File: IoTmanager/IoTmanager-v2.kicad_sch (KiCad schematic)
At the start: 63 parts, among them J2 Conn_01x12_Pin, J3 Conn_01x12_Pin, J4-flash1 flash, J5 reset, K3 ZC32F-012-HS3-copy, K5 ZC32F-012-HS3-copy, K6 ZC32F-012-HS3-copy, K7 ZC32F-012-HS3-copy, Q1-pnp1 MMBT5401, Q10-pnp1 MMBT5401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

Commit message: update
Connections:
- net +12C: now also J2.3 (Pin_3); no longer J2.12 (Pin_12)
- net +3.3V: now also J2.5 (Pin_5)
- net +5C: now also J2.4 (Pin_4); no longer J2.2 (Pin_2)
- net GNDPWR: now also J2.2 (Pin_2)
- net d8: now also J2.12 (Pin_12); no longer J2.5 (Pin_5)
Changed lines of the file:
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@@
 	)
 	(label "d8"
-		(at 264.16 160.02 0)
+		(at 269.24 177.8 0)
 		(fields_autoplaced yes)
 		(effects
@@
 	(symbol
 		(lib_id "power:+12C")
-		(at 269.24 177.8 270)
+		(at 264.16 154.94 270)
 		(unit 1)
 		(exclude_from_sim no)
@@
 		(fields_autoplaced yes)
 		(property "Reference" "#PWR033"
-			(at 265.43 177.8 0)
+			(at 260.35 154.94 0)
 			(effects
 				(font
@@
 		)
 		(property "Value" "+12C"
-			(at 273.05 177.7999 90)
+			(at 267.97 154.9399 90)
 			(effects
 				(font
@@
 		)
 		(property "Footprint" ""
-			(at 269.24 177.8 0)
+			(at 264.16 154.94 0)
 			(effects
 				(font
@@
 		)
 		(property "Datasheet" ""
-			(at 269.24 177.8 0)
+			(at 264.16 154.94 0)
 			(effects
 				(font
@@
 		)
 		(property "Description" "Power symbol creates a global label with name \"+12C\""
-			(at 269.24 177.8 0)
+			(at 264.16 154.94 0)
 			(effects
 				(font
@@
 	)
 	(symbol
+		(lib_id "power:+3.3V")
+		(at 264.16 160.02 270)
+		(unit 1)
+		(exclude_from_sim no)
+		(in_bom yes)
+		(on_board yes)
+		(dnp no)
+		(fields_autoplaced yes)
+		(property "Reference" "#PWR036"
+			(at 260.35 160.02 0)
+			(effects
+				(font
+					(size 1.27 1.27)
+				)
+				(hide yes)
+			)
+		)
+		(property "Value" "+3.3V"
+			(at 267.97 160.0199 90)
+			(effects
+				(font
+					(size 1.27 1.27)
+				)
+				(justify left)
+			)
+		)
+		(property "Footprint" ""
+			(at 264.16 160.02 0)
+			(effects
+				(font
+					(size 1.27 1.27)
+				)
+				(hide yes)
+			)
+		)
+		(property "Datasheet" ""
+			(at 264.16 160.02 0)
+			(effects
+				(font
+					(size 1.27 1.27)
+				)
+				(hide yes)
+			)
+		)
+		(property "Description" "Power symbol creates a global label with name \"+3.3V\""
+			(at 264.16 160.02 0)
+			(effects
+				(font
+					(size 1.27 1.27)
+				)
+				(hide yes)
+			)
+		)
+		(pin "1"
+		)
+		(instances
+			(project "IoTmanager-v2"
+				(path "/e30adb8f-2050-4707-a23b-b56498f87e6f"
+					(reference "#PWR036")
+					(unit 1)
+				)
+			)
+		)
+	)
+	(symbol
 		(lib_id "power:GNDPWR")
 		(at 60.96 71.12 0)
@@
 	)
 	(symbol
+		(lib_id "power:GNDPWR")
+		(at 264.16 152.4 90)
+		(unit 1)
+		(exclude_from_sim no)
+		(in_bom yes)
+		(on_board yes)
+		(dnp no)
+		(fields_autoplaced yes)
+		(property "Reference" "#PWR045"
+			(at 269.24 152.4 0)
+			(effects
+				(font
+					(size 1.27 1.27)
+				)
+				(hide yes)
+			)
+		)
+		(property "Value" "GNDPWR"
+			(at 267.97 152.5269 90)
+			(effects
+				(font
+					(size 1.27 1.27)
+				)
+				(justify right)
+			)
+		)
+		(property "Footprint" ""
+			(at 265.43 152.4 0)
+			(effects
+				(font
+					(size 1.27 1.27)
+				)
+				(hide yes)
+			)
+		)
+		(property "Datasheet" ""
+			(at 265.43 152.4 0)
+			(effects
+				(font
+					(size 1.27 1.27)
+				)
+				(hide yes)
+			)
+		)
+		(property "Description" "Power symbol creates a global label with name \"GNDPWR\" , global ground"
+			(at 264.16 152.4 0)
+			(effects
+				(font
+					(size 1.27 1.27)
+				)
+				(hide yes)
+			)
+		)
+		(pin "1"
+		)
+		(instances
+			(project "IoTmanager-v2"
+				(path "/e30adb8f-2050-4707-a23b-b56498f87e6f"
+					(reference "#PWR045")
+					(unit 1)
+				)
+			)
+		)
+	)
+	(symbol
 		(lib_id "power:+3.3V")
 		(at 182.88 279.4 0)
@@
 	(symbol
 		(lib_id "power:+5C")
-		(at 264.16 152.4 270)
+		(at 264.16 157.48 270)
 		(unit 1)
 		(exclude_from_sim no)
@@
 		(fields_autoplaced yes)
 		(property "Reference" "#PWR09"
-			(at 260.35 152.4 0)
+			(at 260.35 157.48 0)
 			(effects
 				(font
@@
 		)
 		(property "Value" "+5C"
-			(at 267.97 152.3999 90)
+			(at 267.97 157.4799 90)
 			(effects
 				(font
@@
 		)
 		(property "Footprint" ""
-			(at 264.16 152.4 0)
+			(at 264.16 157.48 0)
 			(effects
 				(font
@@
 		)
 		(property "Datasheet" ""
-			(at 264.16 152.4 0)
+			(at 264.16 157.48 0)
 			(effects
 				(font
@@
 		)
 		(property "Description" "Power symbol creates a global label with name \"+5C\""
-			(at 264.16 152.4 0)
+			(at 264.16 157.48 0)
 			(effects
 				(font

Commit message: update
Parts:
- added C2: C_Polarized_1000mF, Capacitor_THT:CP_Radial_D10.0mm_P3.50mm, symbol resistor:C_Polarized_Small
- added D6: LED, LED_THT:LED_D5.0mm, symbol Device:LED
- added R10: R-150, Resistor_SMD:R_0805_2012Metric, symbol models:R-100
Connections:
- net +5C: now also C2.1, D6.2 (A)
- net GNDPWR: now also C2.2, R10.2
- new net: D6.1 (K), R10.1

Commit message: update
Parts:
- added R12-10k2, R12-10k3: R-1k, Resistor_SMD:R_0805_2012Metric, symbol models:R-10k
- added U3: DHT11, Sensor:Aosong_DHT11_5.5x12.0_P2.54mm, symbol Sensor:DHT11
- U1, U4: now not fitted
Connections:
- net +5C: now also U3.1 (VDD)
- net GNDPWR: now also U3.4 (GND)
- net d0: no longer J2.9 (Pin_9)
- net d1: now also U3-tsop23.1 (OUT), R12-10k3.2; no longer U2.20 (GPIO5)
- net d2: now also R12-10k2.2; no longer U2.19 (GPIO4)
- net d4: now also U3.2 (DATA)
- net d5: no longer Jumper-d5.1, U3-tsop23.1 (OUT)
- net d6: no longer Jumper-d6.1
- net d7: no longer Jumper-d7.1
- net at IRLR1.1 (G), R5.2, R6.2: now also Jumper-d6.1
- net at IRLR3.1 (G), R8.2, R9.2: now also Jumper-d7.1
- net at IRLR2.1 (G), R1.2, R2.2: now also Jumper-d5.1
- new net: R12-10k3.1, U2.20 (GPIO5)
- new net: R12-10k2.1, U2.19 (GPIO4)
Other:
- moved on the sheet: IRLR3, Jumper-d5, Jumper-d6, Jumper-d7, R5, R8, R9

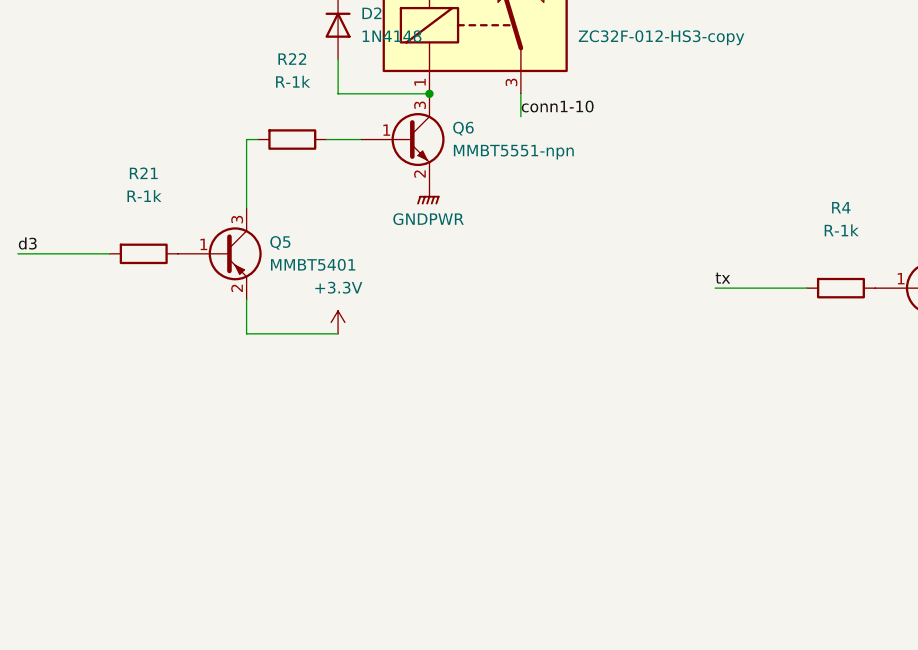
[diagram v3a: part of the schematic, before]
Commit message: Update IoTmanager schematic and libraries
- Changed paper size from A3 to A2 in IoTmanager schematic.
- Added MMDT4413-7-F symbol and footprint to the schematic and libraries.
- Updated various component properties including reference, value, and footprint.
- Adjusted component placements and added new power symbols for +3.3V and GNDPWR.
- Modified existing project files in Proteous tests, including autosaved versions.
- Updated fp-info-cache with new component details.
- Created new KiCAD symbol and footprint files for MMDT4413-7-F.
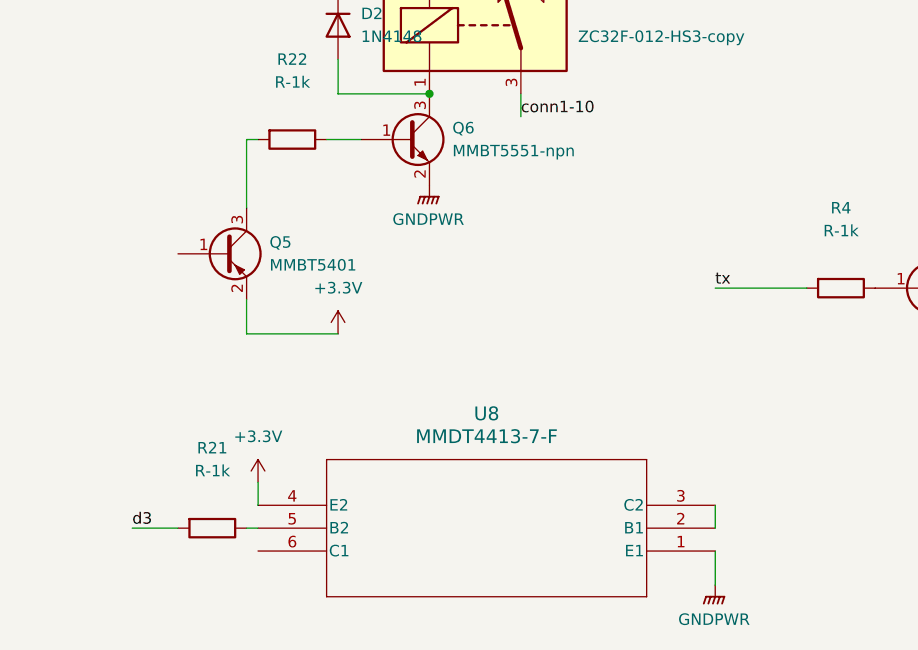
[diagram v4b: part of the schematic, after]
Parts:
- added U8: MMDT4413-7-F, module-custom-for-esp8266:SOT-363_DIO, symbol models:MMDT4413-7-F
- U3-tsop23: footprint OptoDevice:Vishay_MOLD-3Pin -> module-custom-for-esp8266:Vishay_MINIMOLD-3Pin_GND_correct
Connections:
- net +3.3V: now also U8.4 (E2)
- net GNDPWR: now also U8.1 (E1)
- net at R21.1: now also U8.5 (B2); no longer Q5.1 (B)
- new net: U8.2 (B1), U8.3 (C2)
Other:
- moved on the sheet: R21

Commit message: auto update from EPAM computer
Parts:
- added C3: C_Small, Capacitor_SMD:C_0805_2012Metric_Pad1.18x1.45mm_HandSolder, symbol Device:C_Small
- added R11: R-100, Resistor_SMD:R_0805_2012Metric, symbol models:R-100
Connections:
- net +5C: now also C3.1
- net GNDPWR: now also C3.2
- net d1: now also R11.2; no longer U3-tsop23.1 (OUT)
- net d2: now also R16.2
- net d8: no longer R16.2
- new net: R11.1, U3-tsop23.1 (OUT)

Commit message: update
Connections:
- net d3: now also Q5.1 (B)
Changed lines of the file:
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@@
 	(wire
 		(pts
-			(xy 161.29 180.34) (xy 163.83 180.34)
+			(xy 240.03 128.27) (xy 245.11 128.27)
 		)
 		(stroke
@@
 	(wire
 		(pts
-			(xy 240.03 128.27) (xy 245.11 128.27)
+			(xy 138.43 180.34) (xy 153.67 180.34)
 		)
 		(stroke
@@
 	(wire
 		(pts
-			(xy 138.43 180.34) (xy 153.67 180.34)
-		)
-		(stroke
-			(width 0)
-			(type default)
-		)
-	)
-	(wire
-		(pts
 			(xy 140.97 123.19) (xy 148.59 123.19)
 		)
@@
 	(wire
 		(pts
+			(xy 15.24 262.89) (xy 20.32 262.89)
+		)
+		(stroke
+			(width 0)
+			(type default)
+		)
+	)
+	(wire
+		(pts
 			(xy 135.89 248.92) (xy 135.89 251.46)
 		)
@@
 	(wire
 		(pts
+			(xy 163.83 180.34) (xy 161.29 180.34)
+		)
+		(stroke
+			(width 0)
+			(type default)
+		)
+	)
+	(wire
+		(pts
 			(xy 139.7 97.79) (xy 139.7 100.33)
 		)
@@
 		)
 	)
+	(label "d3"
+		(at 15.24 262.89 0)
+		(fields_autoplaced yes)
+		(effects
+			(font
+				(size 1.27 1.27)
+			)
+			(justify left bottom)
+		)
+	)
 	(label "conn2-9"
 		(at 265.43 210.82 0)
@@
 		(on_board yes)
 		(dnp no)
-		(fields_autoplaced yes)
 		(property "Reference" "R21"
-			(at 24.13 284.48 90)
+			(at 24.13 289.052 90)
 			(effects
 				(font
@@
 		)
 		(property "Value" "R-1k"
-			(at 24.13 287.02 90)
+			(at 24.384 290.83 90)
 			(effects
 				(font
@@
 					(size 1.27 1.27)
 				)
+				(hide yes)
 			)
 		)

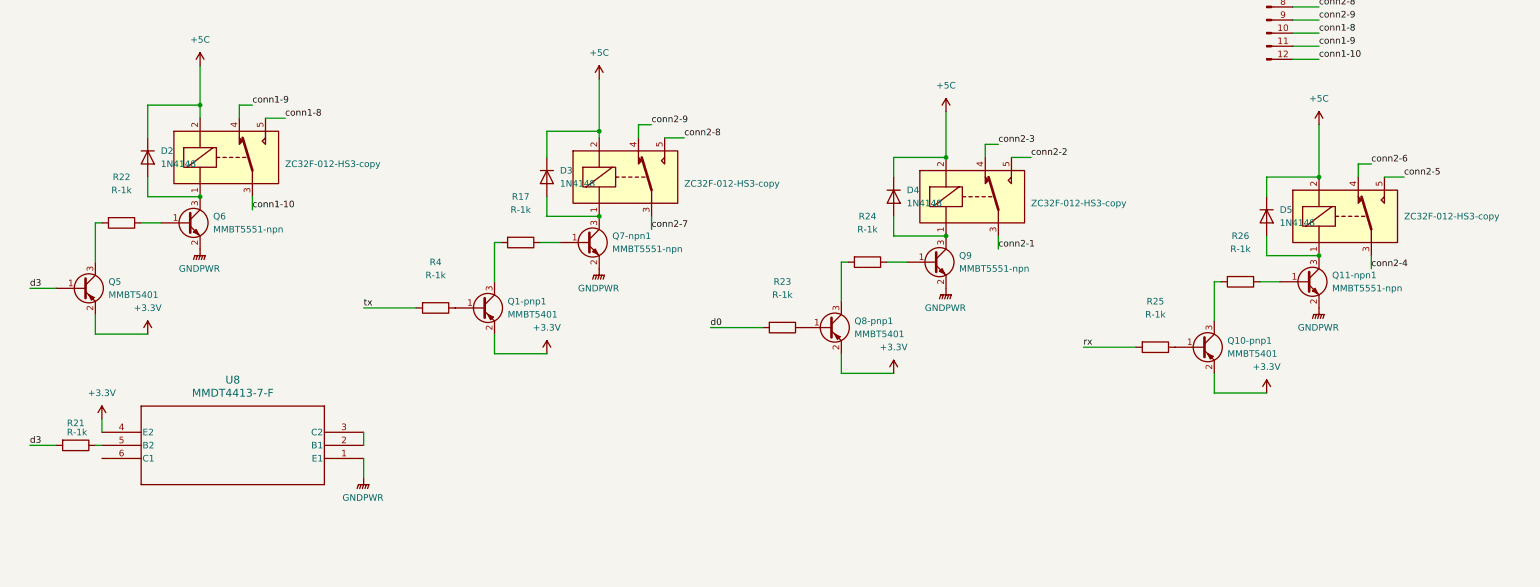
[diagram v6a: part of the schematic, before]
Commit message: Update fp-info-cache with new audio module and relay specifications
- Updated the ID for the Audio_Module entry.
- Added new relay module (RELAY_SRD-05VDC-SL-C) with specifications.
- Ensured proper formatting and consistency in the module entries.
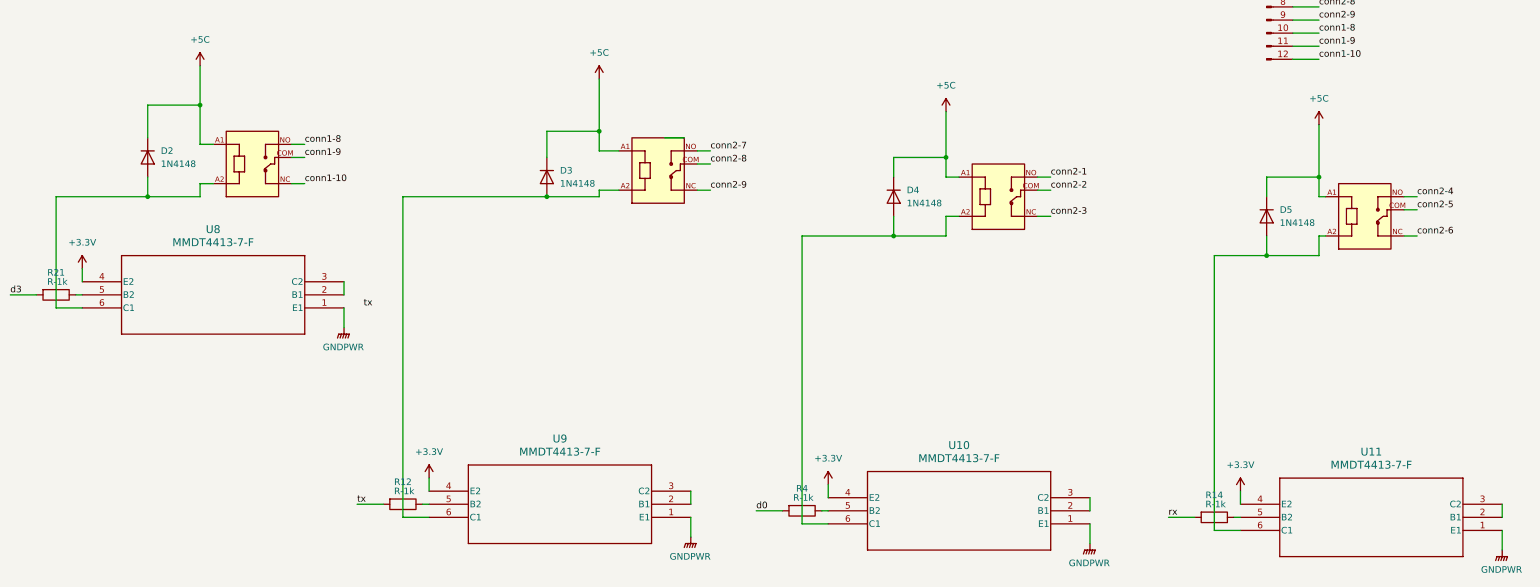
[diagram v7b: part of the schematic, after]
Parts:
- removed Q1-pnp1, Q10-pnp1, Q5, Q8-pnp1: MMBT5401, Package_TO_SOT_SMD:SOT-23, symbol models:MMBT5401-pnp
- removed Q11-npn1, Q6, Q7-npn1, Q9: MMBT5551-npn, Package_TO_SOT_SMD:SOT-23, symbol models:MMBT5551-npn
- removed R17, R22, R23, R24, R25, R26: R-1k, Resistor_SMD:R_0805_2012Metric, symbol models:R-1k
- added R12, R14: R-1k, Resistor_SMD:R_0805_2012Metric, symbol models:R-1k
- added U10, U11, U9: MMDT4413-7-F, module-custom-for-esp8266:SOT-363_DIO, symbol models:MMDT4413-7-F
- K3, K5, K6: footprint module-custom-for-esp8266:HF32F-005-ZS3 -> module-custom-for-esp8266:RELAY_SRD-05VDC-SL-C; symbol models:ZC32F-012-HS3-copy -> models:SRD-05VDC-SL-C; Availability (none) -> In Stock; Check_prices (none) -> https://www.snapeda.com/parts/SRD-05VDC-SL-C/Songle+Relay/v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; Description_1 (none) -> 5V Trigger Relay Module For Arduino And Raspberry Pi 5V Tri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; MANUFACTURER (none) -> SONGLE RELAY; MF (none) -> Songle Relay; MP (none) -> SRD-05VDC-SL-C; Package (none) -> NON STANDARD-5 Songle Relay; Price (none) -> None; STANDARD (none) -> IPC-7251; SnapEDA_Link (none) -> https://www.snapeda.com/parts/SRD-05VDC-SL-C/Songle+Relay/v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
- K7: footprint module-custom-for-esp8266:HF32F-005-ZS3 -> module-custom-for-esp8266:RELAY_SRD-05VDC-SL-C; symbol models:ZC32F-012-HS3 -> models:SRD-05VDC-SL-C; Availability (none) -> In Stock; Check_prices (none) -> https://www.snapeda.com/parts/SRD-05VDC-SL-C/Songle+Relay/v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; Description_1 (none) -> 5V Trigger Relay Module For Arduino And Raspberry Pi 5V Tri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; MANUFACTURER (none) -> SONGLE RELAY; MF (none) -> Songle Relay; MP (none) -> SRD-05VDC-SL-C; Package (none) -> NON STANDARD-5 Songle Relay; Price (none) -> None; STANDARD (none) -> IPC-7251; SnapEDA_Link (none) -> https://www.snapeda.com/parts/SRD-05VDC-SL-C/Songle+Relay/v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
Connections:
- net +3.3V: now also U10.4 (E2), U11.4 (E2), U9.4 (E2)
- net +5C: now also K3.A1, K5.A1, K6.A1, K7.A1; no longer K3.2, K5.2, K6.2, K7.2
- net GNDPWR: now also U10.1 (E1), U11.1 (E1), U9.1 (E1)
- net conn1-10: now also K3.NC; no longer K3.3
- net conn1-8: now also K3.NO; no longer K3.5
- net conn1-9: now also K3.COM; no longer K3.4
- net conn2-1: now also K6.NO; no longer K6.3
- net conn2-2: now also K6.COM; no longer K6.5
- net conn2-3: now also K6.NC; no longer K6.4
- net conn2-4: now also K7.NO; no longer K7.3
- net conn2-5: now also K7.COM; no longer K7.5
- net conn2-6: now also K7.NC; no longer K7.4
- net conn2-7: now also K5.NO; no longer K5.3
- net conn2-8: now also K5.COM; no longer K5.5
- net conn2-9: now also K5.NC; no longer K5.4
- net d0: now also R4.2
- net rx: now also R14.2
- net tx: now also R12.2; no longer R4.2
- net at D4.2 (A): now also K6.A2, U10.6 (C1); no longer K6.1
- net at D5.2 (A): now also K7.A2, U11.6 (C1); no longer K7.1
- net at D3.2 (A): now also K5.A2, U9.6 (C1); no longer K5.1
- net at D2.2 (A): now also K3.A2, U8.6 (C1); no longer K3.1
- net at R4.1: now also U10.5 (B2)
- new net: R12.1, U9.5 (B2)
- new net: R14.1, U11.5 (B2)
- new net: U10.2 (B1), U10.3 (C2)
- new net: U9.2 (B1), U9.3 (C2)
- new net: U11.2 (B1), U11.3 (C2)
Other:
- moved on the sheet: R21, U8

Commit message: auto update from EPAM computer
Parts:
- D6, MX-RM-5V-RF-sensor1, R10, display/ads1, max1: now not fitted; now left out of the parts list
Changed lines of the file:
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@@
 		(at 160.02 106.68 0)
 		(unit 1)
-		(exclude_from_sim no)
-		(in_bom yes)
-		(on_board yes)
-		(dnp no)
+		(exclude_from_sim yes)
+		(in_bom no)
+		(on_board no)
+		(dnp yes)
 		(fields_autoplaced yes)
 		(property "Reference" "display/ads1"
@@
 		(at 179.07 144.78 0)
 		(unit 1)
-		(exclude_from_sim no)
-		(in_bom yes)
-		(on_board yes)
-		(dnp no)
+		(exclude_from_sim yes)
+		(in_bom no)
+		(on_board no)
+		(dnp yes)
 		(fields_autoplaced yes)
 		(property "Reference" "MX-RM-5V-RF-sensor1"
@@
 		(at 135.89 128.27 0)
 		(unit 1)
-		(exclude_from_sim no)
-		(in_bom yes)
-		(on_board yes)
-		(dnp no)
+		(exclude_from_sim yes)
+		(in_bom no)
+		(on_board no)
+		(dnp yes)
 		(fields_autoplaced yes)
 		(property "Reference" "max1"
@@
 		(at 194.31 31.75 180)
 		(unit 1)
-		(exclude_from_sim no)
-		(in_bom yes)
-		(on_board yes)
-		(dnp no)
+		(exclude_from_sim yes)
+		(in_bom no)
+		(on_board no)
+		(dnp yes)
 		(fields_autoplaced yes)
 		(property "Reference" "D6"
@@
 		(at 201.93 31.75 90)
 		(unit 1)
-		(exclude_from_sim no)
-		(in_bom yes)
-		(on_board yes)
-		(dnp no)
+		(exclude_from_sim yes)
+		(in_bom no)
+		(on_board no)
+		(dnp yes)
 		(fields_autoplaced yes)
 		(property "Reference" "R10"
